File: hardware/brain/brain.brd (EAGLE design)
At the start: 100 x 80 mm, 11 parts, among them IC1 LD117AS33TR, IC2 ESP12

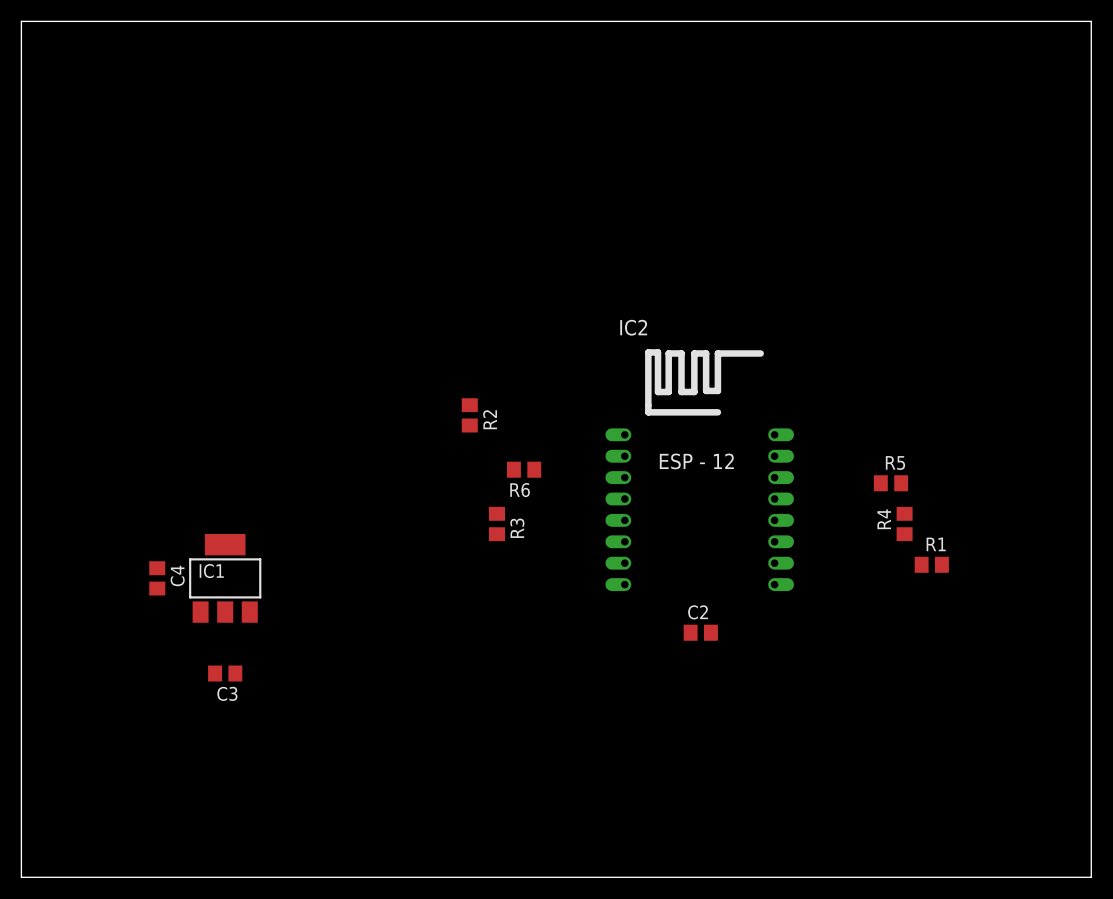
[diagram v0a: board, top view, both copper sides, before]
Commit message: add rtc
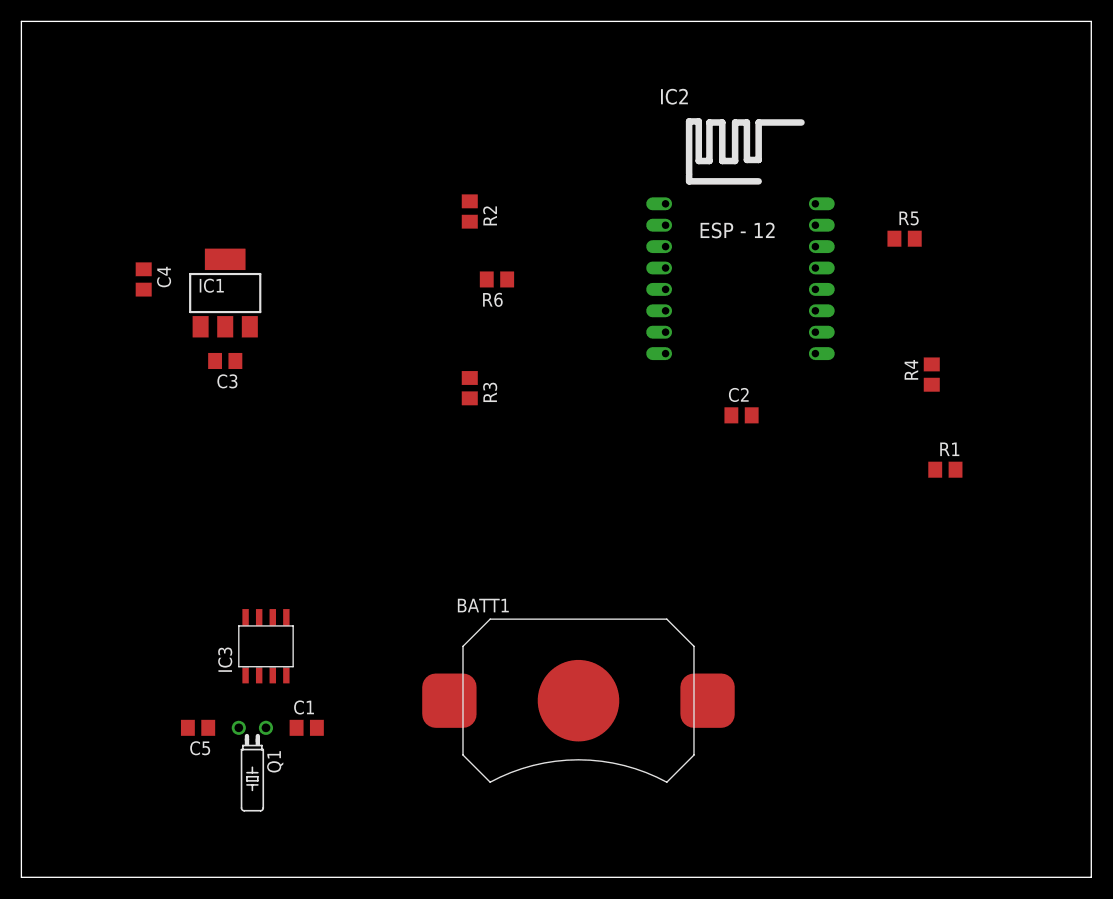
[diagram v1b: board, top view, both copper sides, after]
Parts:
- added BATT1: BATTERY_2032, dp_devices:BATT2032
- added C1, C5: 8p, rcl:C0805
- added IC3: IC_RTC_DS1307, dp_devices:SO-8
- added Q1: 32.768KHz, crystal:TC26H
- moved C3 29.2 mm to (19.1, 48.3)
- moved C4 28.0 mm to (11.4, 55.9)
- moved IC1 26.7 mm to (19.1, 54.6)
- moved R5 22.9 mm to (82.5, 59.7)
- moved IC2 21.9 mm to (67.3, 57.1)
- moved C2 20.7 mm to (67.3, 43.2)
- moved R2 19.0 mm to (41.9, 62.2)
- moved R6 18.0 mm to (44.5, 55.9)
- moved R4 14.2 mm to (85.1, 47.0)
- moved R3 13.0 mm to (41.9, 45.7)
- moved R1 8.98 mm to (86.4, 38.1)
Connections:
- new net N$5: IC3.7
- new net N$6: C5.1, IC3.1, Q1.2
- new net N$7: BATT1.V1, BATT1.V2, IC3.3
- new net N$8: C1.1, IC3.2, Q1.1
- net GND: now also BATT1.V-, C1.2, C5.2, IC3.4
- net SCK: now also IC3.6
- net SDA: now also IC3.5
- net VCC: now also IC3.8

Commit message: edit pin settings, add ch_pd pullup
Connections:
- net N$3 renamed BOOTMODE
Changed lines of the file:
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@@
 <wire x1="87.31" y1="38.1" x2="74.21" y2="50.95" width="0" layer="19" extent="1-1"/>
 </signal>
-<signal name="N$3">
+<signal name="BOOTMODE">
 <contactref element="IC2" pad="GPIO0"/>
 <contactref element="R5" pad="1"/>
